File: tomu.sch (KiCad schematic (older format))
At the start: 17 parts, among them P1 USART0, P2 DEBUG, P3 USB-PCB, P4 RESET_PAD, P5 5V_PAD, U1 EFM32HG309

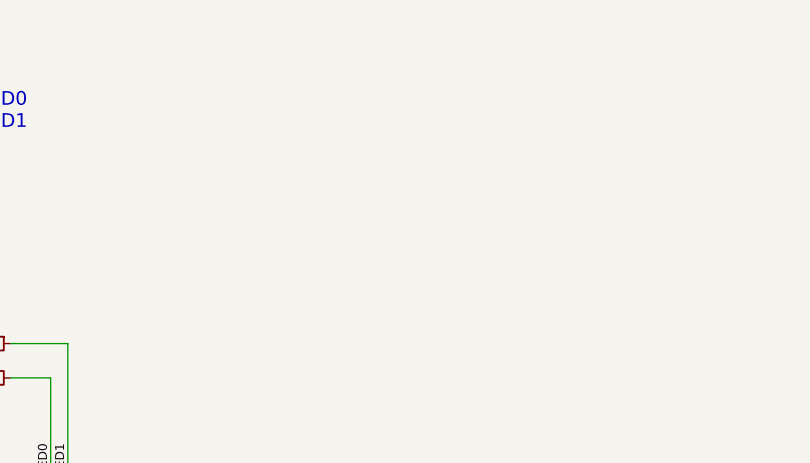
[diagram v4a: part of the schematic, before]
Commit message: hardware: fix outline, replace phantom pad with real one
There was a phantom pad that was created with an external graphic.  It's
unselectable in Kicad, and is weird.  This pad exposes the soldermask on
the captouch buttons.

Recreate it as a real item.

Additionally, fix the graphic outline.

Additionally, move everything up to the corner, to fix drill files later
on.

Signed-off-by: Sean Cross <sean@xobs.io>
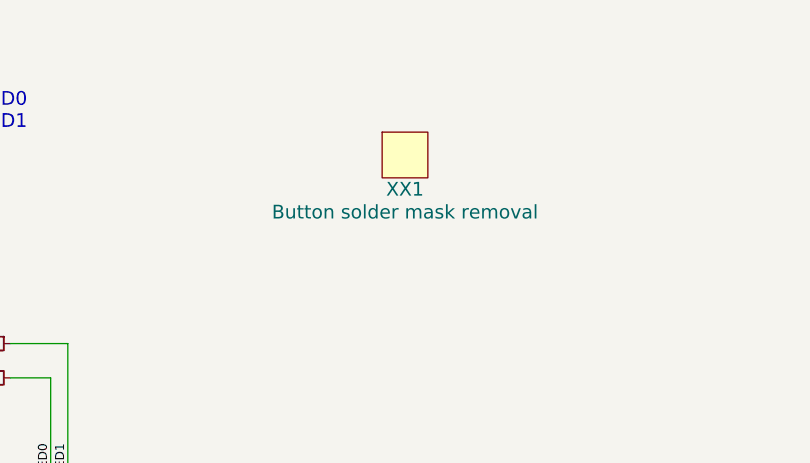
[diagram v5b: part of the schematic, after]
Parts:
- added XX1: Button solder mask removal, usb-pcb:soldermask-removal, symbol Note
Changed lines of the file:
@@
 	7070 3370 7000 3370
 Connection ~ 7000 3370
+$Comp
+L Note XX1
+U 1 1 5A5A1619
+P 5650 1350
+F 0 "XX1" H 5650 1350 60  0000 C CNN
+F 1 "Button solder mask removal" H 5650 1250 60  0000 C CNN
+F 2 "usb-pcb:soldermask-removal" H 5650 1350 60  0001 C CNN
+F 3 "" H 5650 1350 60  0001 C CNN
+	1    5650 1350
+	1    0    0    -1
+$EndComp
 $EndSCHEMATC

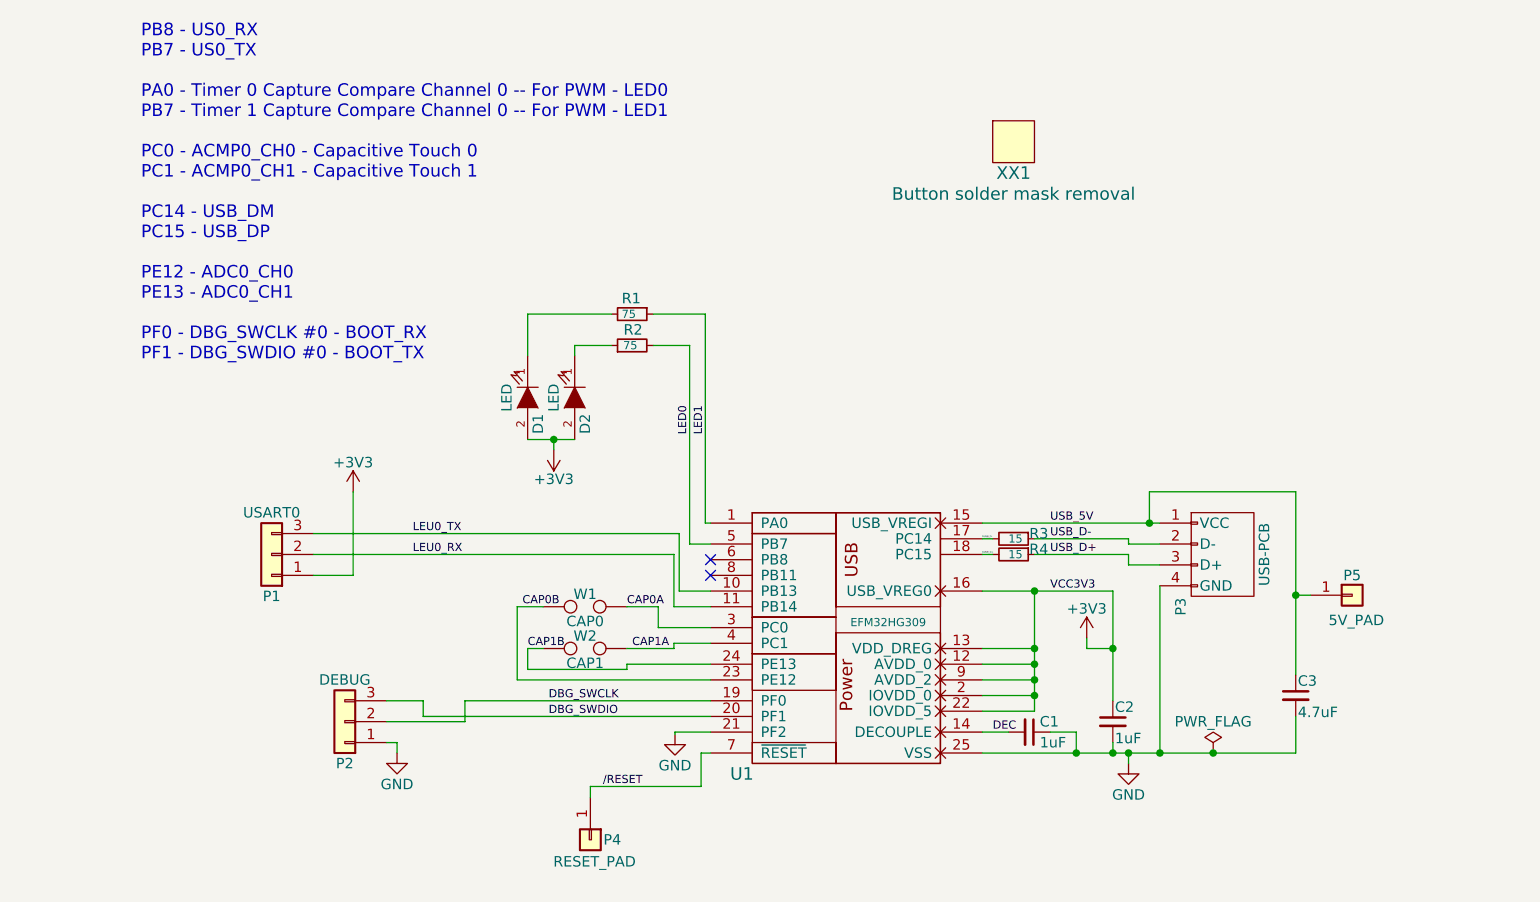
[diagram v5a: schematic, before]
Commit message: schematic: line up to 50 mil spacing
Some components weren't on 50 mil spacing, making it hard to work
with.  Line everything (but the MCU) up to large spacing.

Signed-off-by: Sean Cross <sean@xobs.io>
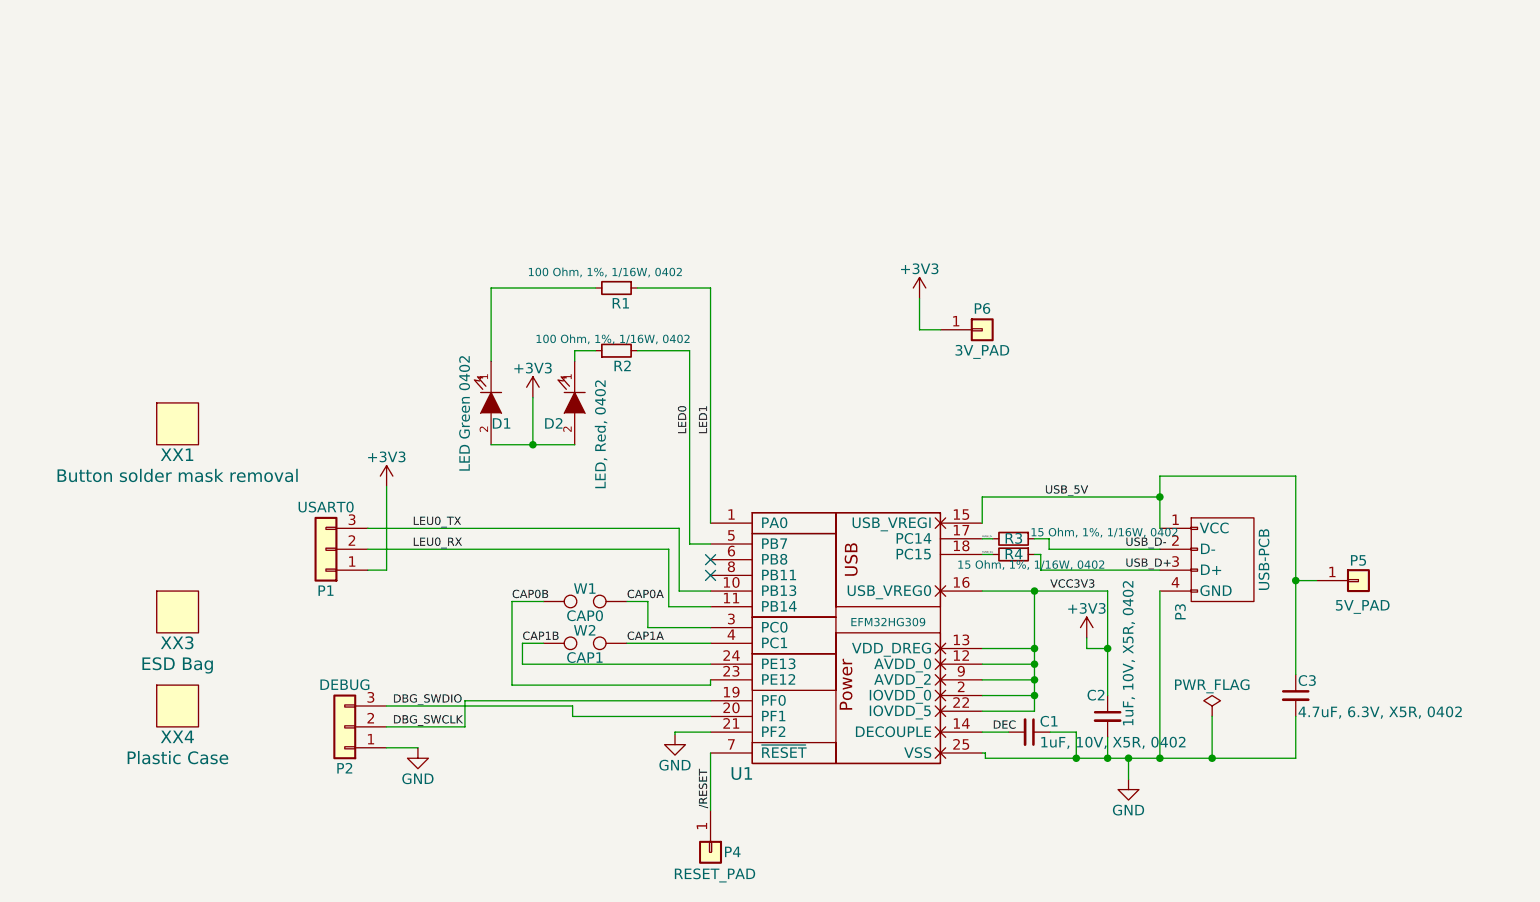
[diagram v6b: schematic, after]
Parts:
- added P6: 3V_PAD, usb-pcb:pads-1x1, symbol Conn_01x01
- added XX3: ESD Bag, symbol Note
- added XX4: Plastic Case, symbol Note
- C1, C2: value 1uF -> 1uF, 10V, X5R, 0402
- C3: value 4.7uF -> 4.7uF, 6.3V, X5R, 0402
- D1: value LED -> LED Green 0402
- D2: value LED -> LED, Red, 0402
- P1: Description (none) -> Test points for serial; Notes (none) -> DNP
- P2: Description (none) -> Test points for SWD; Notes (none) -> DNP
- P3: Description (none) -> USB pads on bottom of PCB; Notes (none) -> DNP
- P4: Description (none) -> Test point for RESET line; Notes (none) -> DNP
- P5: Description (none) -> Test point for supplying 5V power; Notes (none) -> DNP
- R1, R2: value 75 -> 100 Ohm, 1%, 1/16W, 0402
- R3, R4: value 15 -> 15 Ohm, 1%, 1/16W, 0402
- W1, W2: Description (none) -> Capacitive touch pads; Notes (none) -> DNP
- XX1: Description (none) -> Internal component to expose captouch pads; Notes (none) -> DNP
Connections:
- net +3V3: now also P6.1 (Pin_1)
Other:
- note removed: "PB8 - US0_RX\nPB7 - US0_TX\n\nPA0 - Timer 0 Capture Compare Channel 0 -- For PWM - LED0 \nPB7 - Timer 1 Capture Compare Channel 0 -- For PWM - LED1\n\nPC0 - ACMP0_CH0 - Capacitive Touch 0\nPC1 - ACMP0_CH1 - Capacitive Touch 1\n\nPC14 - USB_DM\nPC15 - USB_DP\n\nPE12 - ADC0_CH0\nPE13 - ADC0_CH1\n\nPF0 - DBG_SWCLK #0 - BOOT_RX\nPF1 - DBG_SWDIO #0 - BOOT_TX\n\n"
- moved on the sheet: C2, D1, D2, P1, P2, P3, P4, P5, R1, R2, W1, W2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
